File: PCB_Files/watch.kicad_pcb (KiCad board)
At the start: 2 copper layers, 40.3 x 40.3 mm, 117 parts, among them J1 USB_C_Receptacle_USB2.0_16P, J2 Conn_01x15_MountingPin, J3 Conn_01x02_Pin, Q1 BC847, Q2 BC847, Q3 FS8205A, Q4 BSS138, Q5 BSS138, Q6 BSS138, Q7 BSS138, Q8 BC847, SW1 SW_Push, U10 LSM6DS3, U11 MAX-M10S, U12 MCP1700x-120xxMB, U13 DRV2605LDGS, U2 ESP32-PICO-D4, U3 CP2102N-Axx-xQFN28, U4 TPS7A0533PDBV, U5 MCP73831-2-OT, U6 AP9101CK6, U7 MAX30105EFD_T, U8 W25Q128JVS, U9 BMP388, Y1 SG-3030CM

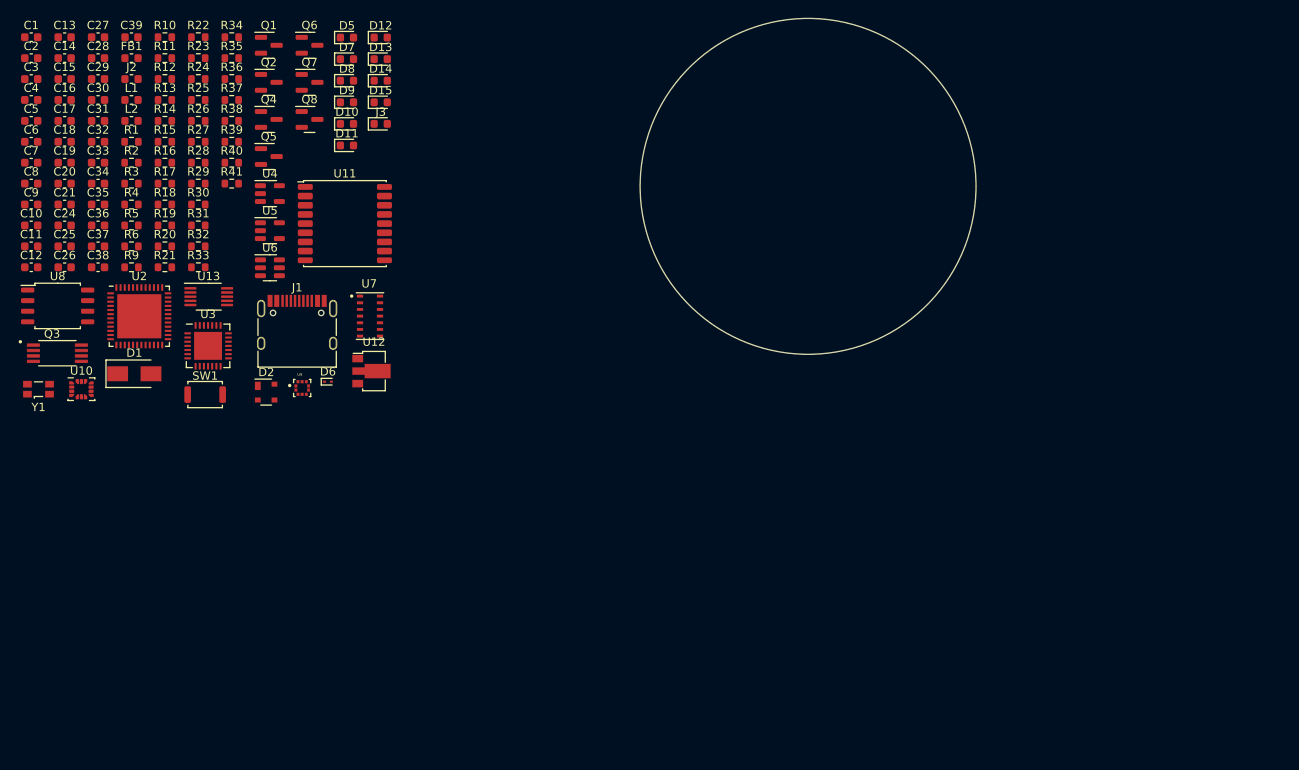
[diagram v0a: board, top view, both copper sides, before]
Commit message: Set trace widths
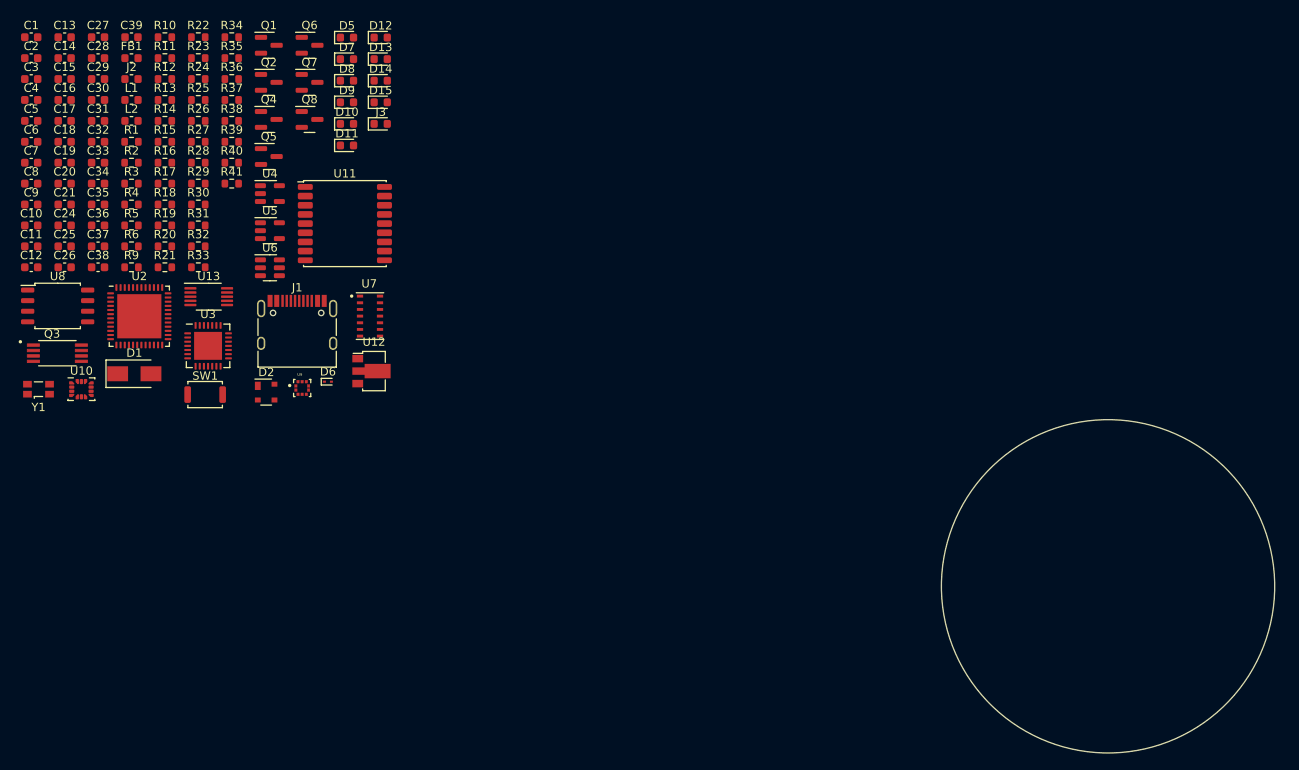
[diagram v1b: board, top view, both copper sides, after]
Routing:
- added copper zone on In2.Cu, net /3V3
- added copper zone on In1.Cu, net GND
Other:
- board size 40.3 x 40.3 mm -> 40 x 40 mm
- copper layers 2 -> 4
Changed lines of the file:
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@@
 	(layers
 		(0 "F.Cu" signal)
+		(4 "In1.Cu" power)
+		(6 "In2.Cu" power)
 		(2 "B.Cu" signal)
 		(9 "F.Adhes" user "F.Adhesive")
@@
 	)
 	(setup
+		(stackup
+			(layer "F.SilkS"
+				(type "Top Silk Screen")
+			)
+			(layer "F.Paste"
+				(type "Top Solder Paste")
+			)
+			(layer "F.Mask"
+				(type "Top Solder Mask")
+				(thickness 0.01)
+			)
+			(layer "F.Cu"
+				(type "copper")
+				(thickness 0.035)
+			)
+			(layer "dielectric 1"
+				(type "prepreg")
+				(thickness 0.1)
+				(material "FR4")
+				(epsilon_r 4.5)
+				(loss_tangent 0.02)
+			)
+			(layer "In1.Cu"
+				(type "copper")
+				(thickness 0.035)
+			)
+			(layer "dielectric 2"
+				(type "core")
+				(thickness 1.24)
+				(material "FR4")
+				(epsilon_r 4.5)
+				(loss_tangent 0.02)
+			)
+			(layer "In2.Cu"
+				(type "copper")
+				(thickness 0.035)
+			)
+			(layer "dielectric 3"
+				(type "prepreg")
+				(thickness 0.1)
+				(material "FR4")
+				(epsilon_r 4.5)
+				(loss_tangent 0.02)
+			)
+			(layer "B.Cu"
+				(type "copper")
+				(thickness 0.035)
+			)
+			(layer "B.Mask"
+				(type "Bottom Solder Mask")
+				(thickness 0.01)
+			)
+			(layer "B.Paste"
+				(type "Bottom Solder Paste")
+			)
+			(layer "B.SilkS"
+				(type "Bottom Silk Screen")
+			)
+			(copper_finish "None")
+			(dielectric_constraints no)
+		)
 		(pad_to_mask_clearance 0)
 		(allow_soldermask_bridges_in_footprints no)
@@
 	)
 	(gr_circle
-		(center 114 52)
-		(end 122 70.5)
+		(center 150 100)
+		(end 170 100)
 		(stroke
 			(width 0.05)
-			(type default)
+			(type solid)
 		)
 		(fill no)
 		(layer "Edge.Cuts")
 	)
+	(zone
+		(net 1)
+		(net_name "GND")
+		(layer "In1.Cu")
+		(hatch edge 0.5)
+		(connect_pads
+			(clearance 0.5)
+		)
+		(min_thickness 0.2)
+		(filled_areas_thickness no)
+		(fill yes
+			(thermal_gap 0.5)
+			(thermal_bridge_width 0.5)
+		)
+		(polygon
+			(pts
+				(xy 129.5 80) (xy 170 80) (xy 170 119.5) (xy 130 120)
+			)
+		)
+	)
+	(zone
+		(net 2)
+		(net_name "/3V3")
+		(layer "In2.Cu")
+		(hatch edge 0.5)
+		(priority 1)
+		(connect_pads
+			(clearance 0.5)
+		)
+		(min_thickness 0.2)
+		(filled_areas_thickness no)
+		(fill yes
+			(thermal_gap 0.5)
+			(thermal_bridge_width 0.5)
+		)
+		(polygon
+			(pts
+				(xy 170 80) (xy 170 119.5) (xy 130 120) (xy 129.5 80)
+			)
+		)
+	)
 	(embedded_fonts no)

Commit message: Update PCB layout and project settings
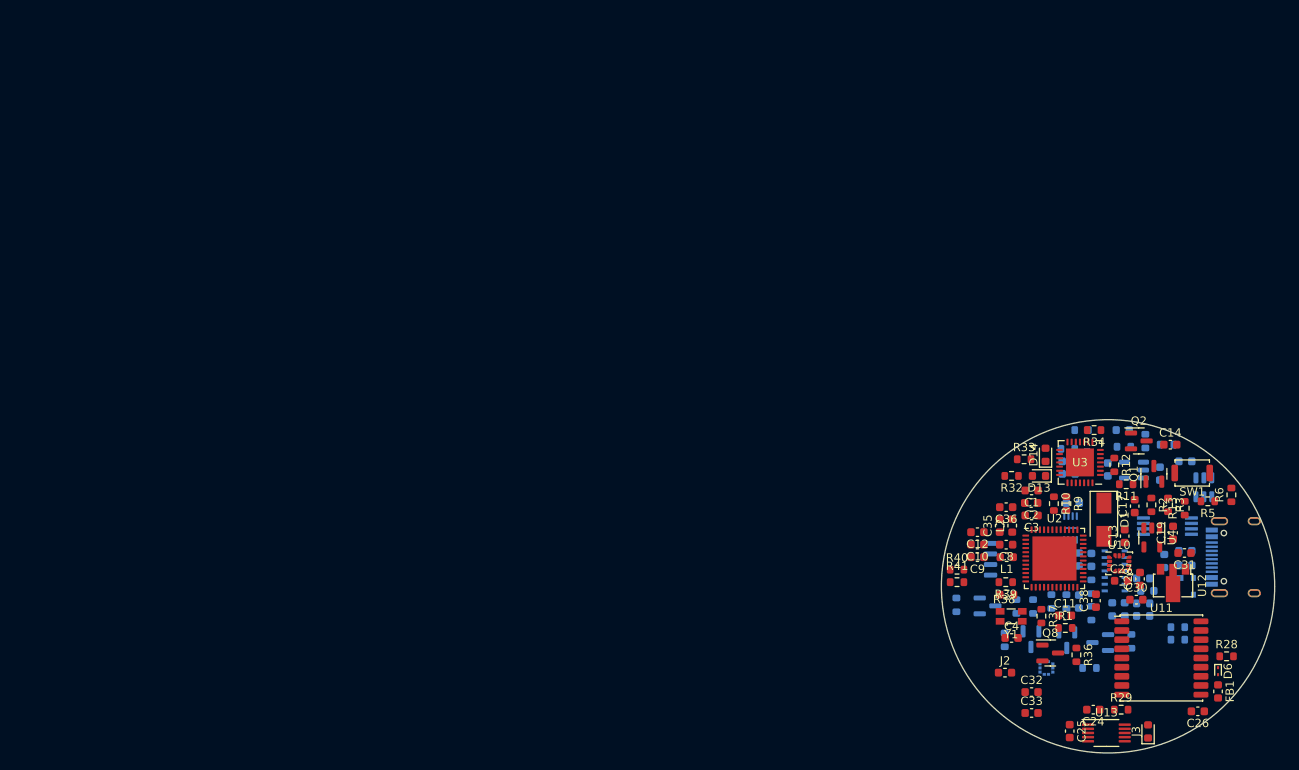
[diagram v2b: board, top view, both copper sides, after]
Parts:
- added U1: APS6404L-3SQRx-ZR, Package_SON:Winbond_USON-8-1EP_3x2mm_P0.5mm_EP0.2x1.6mm, B.Cu at (145.5, 93.0)
- C15, C16, C18, C20, C21, C29, C34, C37, C39, C5, C6, C7, D10, D11, D12, D15, D2, D5, D7, D8, D9, J1, Q3, Q4, Q5, Q6, Q7, R14, R15, R16, R17, R18, R19, R20, R21, R22, R23, R24, R25, R26, R27, R30, R31, R35, R4, U5, U6, U7, U9: moved to B.Cu
- U8: footprint Package_SO:SOIC-8_5.23x5.23mm_P1.27mm -> footprints:SOIC-8_5.23x5.23mm_P1.27mm; moved to B.Cu
- moved FB1 150.9 mm to (163.2, 112.6), turned to -90 degrees
- moved C15 146.6 mm to (159.3, 97.5)
- moved C26 146.1 mm to (160.8, 115.0), turned to 180 degrees
- moved C16 145.0 mm to (159.3, 95.8)
- moved C5 144.4 mm to (159.3, 85.0), turned to 180 degrees
- moved C13 140.6 mm to (152.0, 94.0), turned to 90 degrees
- moved C14 140.6 mm to (157.5, 83.0)
- moved C7 140.5 mm to (156.2, 86.5), turned to 90 degrees
- moved C31 140.3 mm to (159.2, 96.0), turned to 180 degrees
- moved C19 140.2 mm to (157.8, 93.6), turned to 90 degrees
- moved C28 139.8 mm to (153.8, 99.1), turned to 90 degrees
- moved C27 139.0 mm to (151.6, 99.3)
- moved C30 138.3 mm to (153.4, 101.6)
- moved R28 136.9 mm to (164.2, 108.4)
- moved C17 136.5 mm to (153.2, 90.4), turned to 90 degrees
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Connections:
- U8 pad 4: unconnected-(U8-GND-Pad4) -> GND

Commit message: Changes in schematics
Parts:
- J1: moved to F.Cu
- moved J1 3.53 mm to (167.0, 100.0), turned to 90 degrees
- moved U11 0.95 mm to (155.4, 108.6)
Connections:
- U8 pad 4: GND -> unconnected-(U8-GND-Pad4)
